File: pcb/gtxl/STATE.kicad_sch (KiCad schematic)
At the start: 7 parts, among them U11 74LS299, U17 74LS377, U18 74LS574, U30 74AHCT04

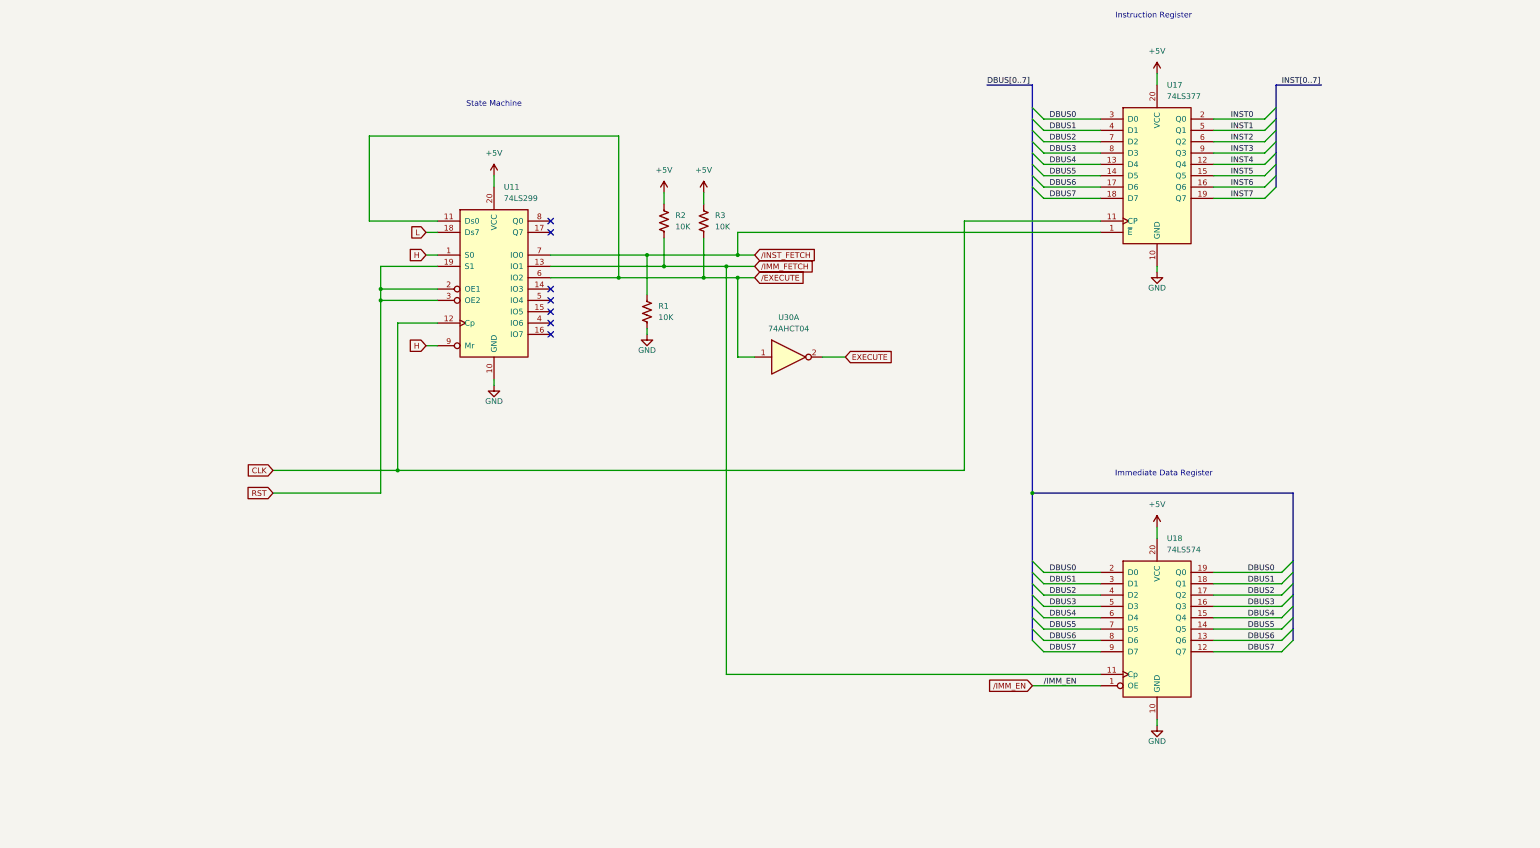
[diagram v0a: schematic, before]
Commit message: Update schematic with removed timer.  Update video timing notes.
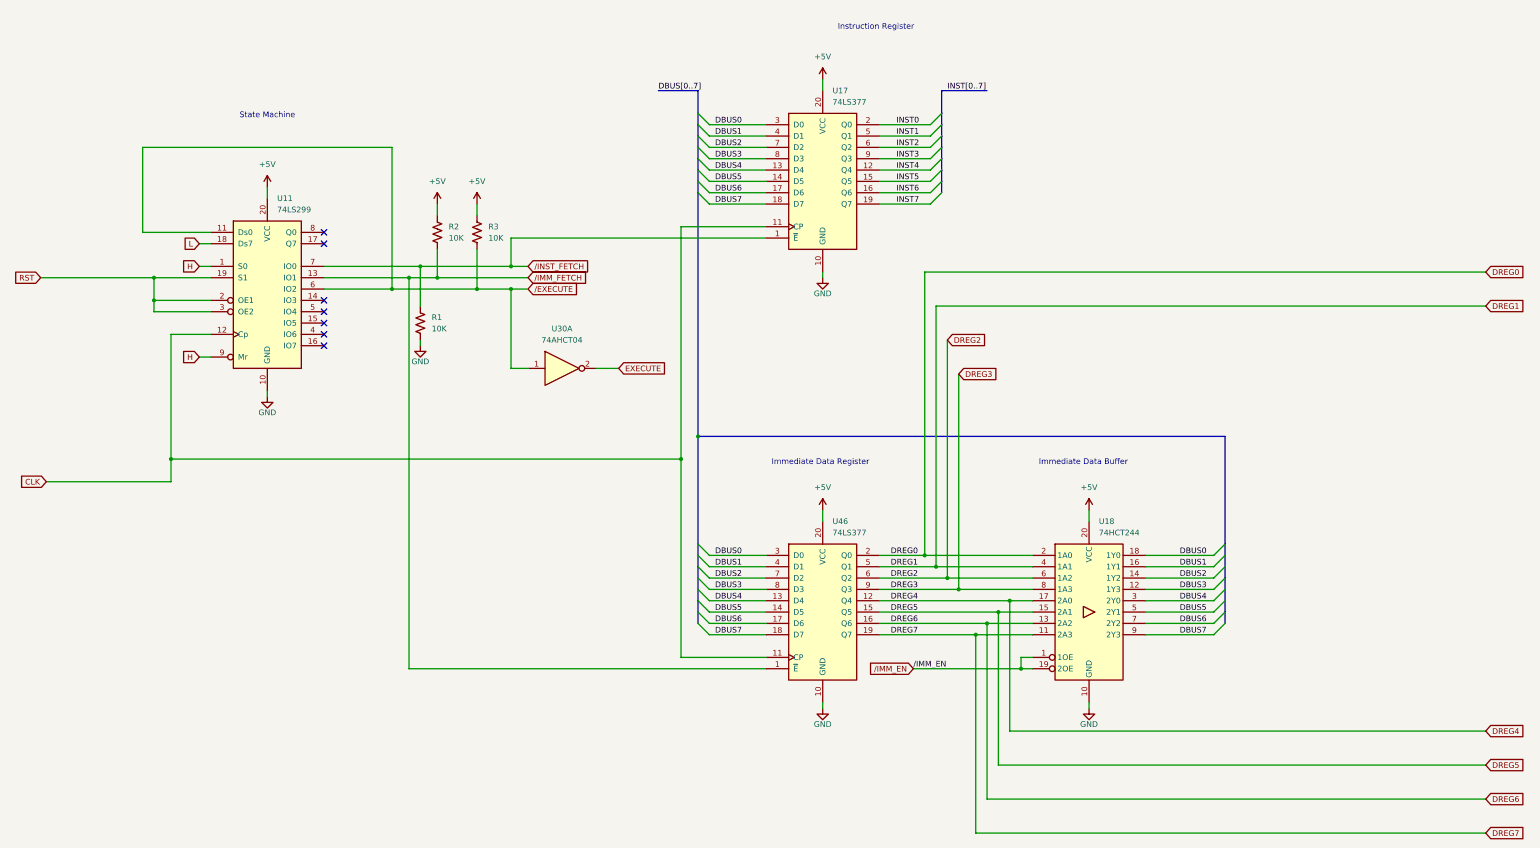
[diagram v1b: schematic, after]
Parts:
- removed U18: 74LS574, symbol 74xx:74LS574
- added U18: 74HCT244, symbol 74xx:74HCT244
- added U46: 74LS377, symbol 74xx:74LS377
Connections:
- net +5V: now also U18.20 (VCC), U46.20 (VCC)
- net CLK: now also U46.11 (CP)
- net DBUS0: now also U18.18 (1Y0), U46.3 (D0)
- net DBUS1: now also U18.16 (1Y1), U46.4 (D1)
- net DBUS2: now also U18.14 (1Y2), U46.7 (D2)
- net DBUS3: now also U18.12 (1Y3), U46.8 (D3)
- net DBUS4: now also U18.3 (2Y0), U46.13 (D4)
- net DBUS5: now also U18.5 (2Y1), U46.14 (D5)
- net DBUS6: now also U18.7 (2Y2), U46.17 (D6)
- net DBUS7: now also U18.9 (2Y3), U46.18 (D7)
- net GND: now also U18.10 (GND), U46.10 (GND)
- net /IMM_EN: now also U18.1 (1OE), U18.19 (2OE)
- net /IMM_FETCH: now also U46.1 (~{E})
- new net DREG0: U18.2 (1A0), U46.2 (Q0)
- new net DREG1: U18.4 (1A1), U46.5 (Q1)
- new net DREG2: U18.6 (1A2), U46.6 (Q2)
- new net DREG3: U18.8 (1A3), U46.9 (Q3)
- new net DREG4: U18.17 (2A0), U46.12 (Q4)
- new net DREG5: U18.15 (2A1), U46.15 (Q5)
- new net DREG6: U18.13 (2A2), U46.16 (Q6)
- new net DREG7: U18.11 (2A3), U46.19 (Q7)
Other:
- note added: "Immediate Data Buffer"
- moved on the sheet: R1, R2, R3, U11, U17, U30A
